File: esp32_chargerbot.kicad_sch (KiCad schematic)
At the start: 6 parts, among them J1 USB_C_Receptacle_USB2.0_16P, U1 AMS1117-3.3

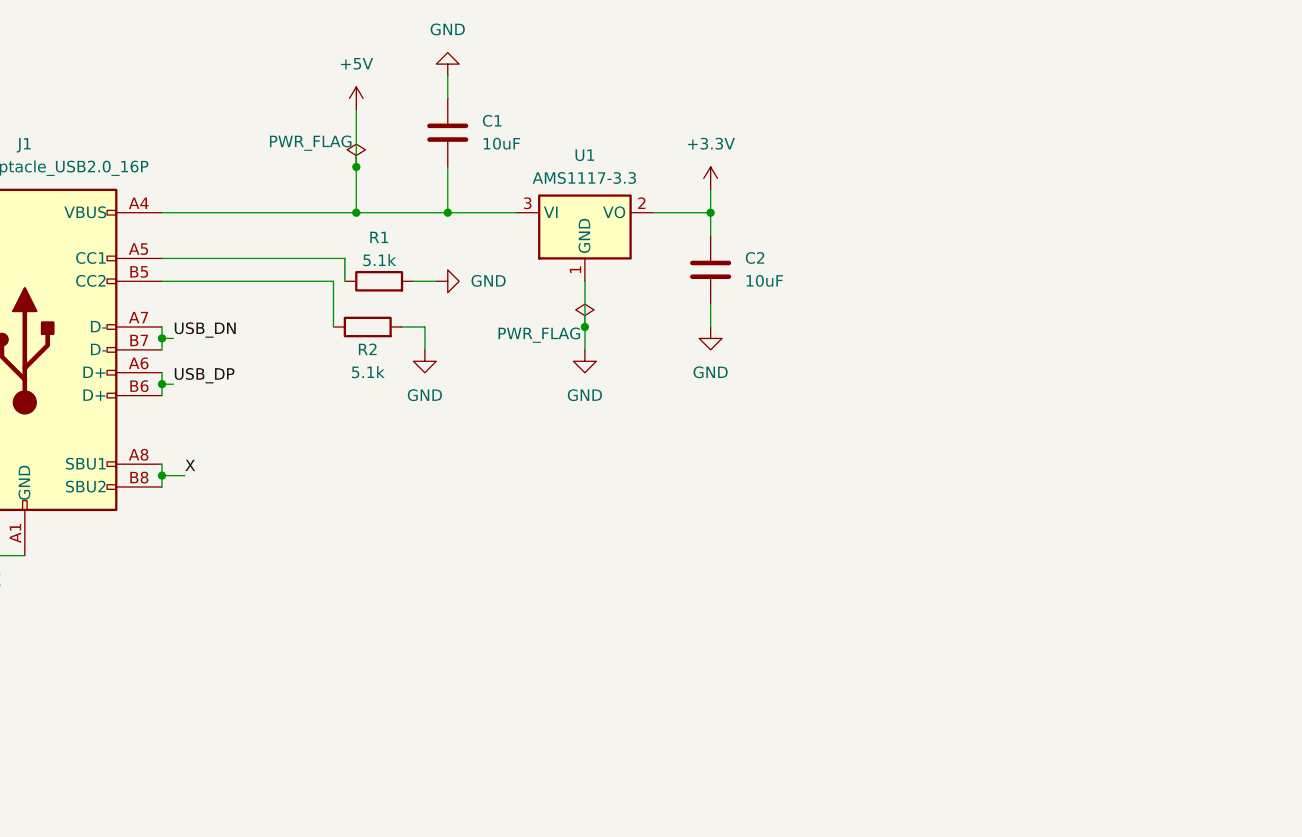
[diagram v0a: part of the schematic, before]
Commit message: ESP32-S3 power wiring, USB D+/D- fix
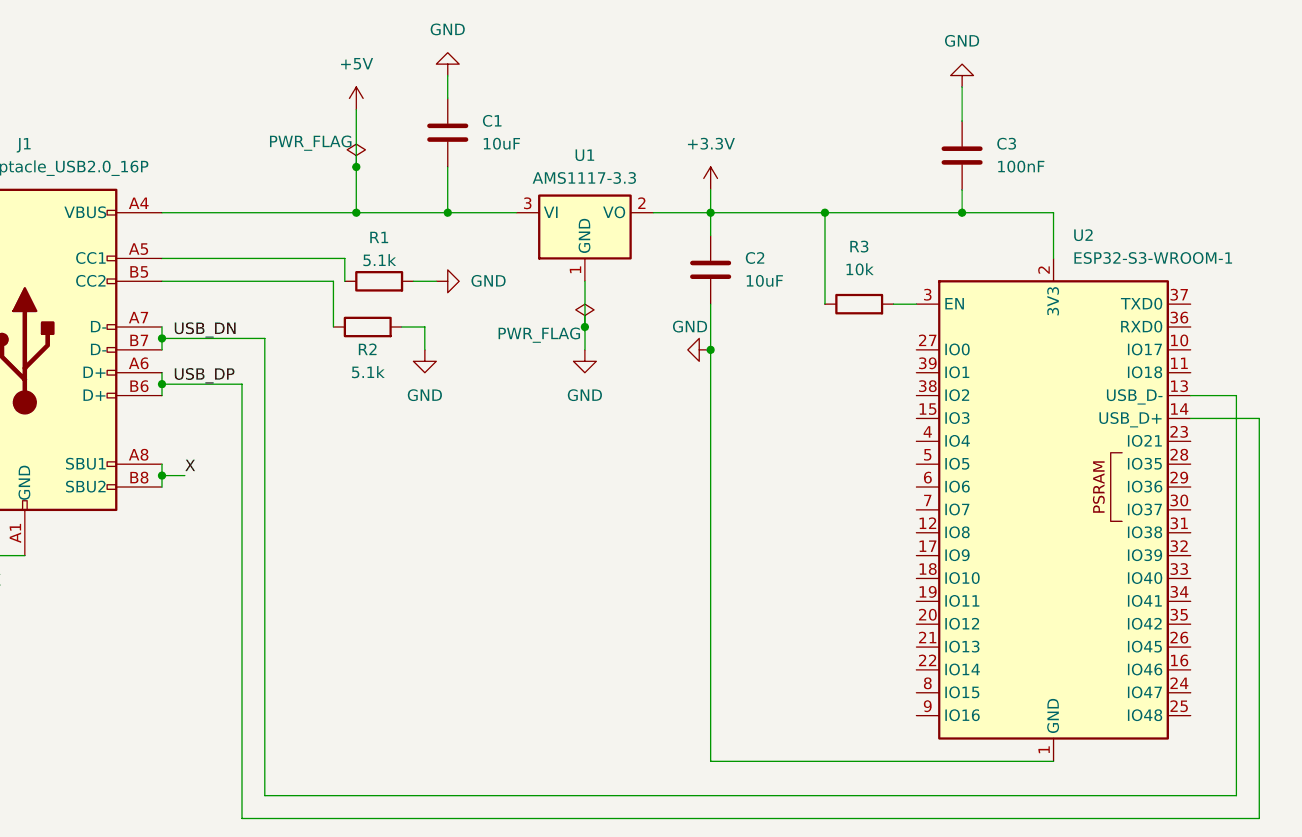
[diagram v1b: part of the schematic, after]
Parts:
- added C3: 100nF, symbol Device:C
- added R3: 10k, symbol Device:R
- added U2: ESP32-S3-WROOM-1, RF_Module:ESP32-S3-WROOM-1, symbol RF_Module:ESP32-S3-WROOM-1
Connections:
- net +3.3V: now also C3.1, R3.1, U2.2 (3V3)
- net GND: now also C3.2, U2.1 (GND), U2.40 (GND), U2.41 (GND)
- net USB_DN: now also U2.13 (USB_D-)
- net USB_DP: now also U2.14 (USB_D+)
- new net: R3.2, U2.3 (EN)

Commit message: MPU-6050 wiring complete, previous errors fixed
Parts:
- added C4: 0.1uF, symbol Device:C
- added C5: 2.2nF, symbol Device:C
- added C6: 10nF, symbol Device:C
- added R4: 10k, symbol Device:R
- added R5, R6: 4.7k, symbol Device:R
- added SW1, SW2: SW_Push, symbol Switch:SW_Push
- added U4: MPU-6050, Sensor_Motion:InvenSense_QFN-24_4x4mm_P0.5mm, symbol Sensor_Motion:MPU-6050
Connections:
- net +3.3V: now also C6.1, R4.2, R5.2, R6.2, U4.13 (VDD), U4.8 (VLOGIC)
- net GND: now also C4.1, C5.1, C6.2, SW1.1, SW2.1, U4.11 (FSYNC), U4.18 (GND), U4.9 (AD0)
- net at R3.2, U2.3 (EN): now also SW1.2
- net SDA: now reaches U2.12 (IO8)
- net SDA: now also R5.1, U4.24 (SDA)
- net SCL: now reaches U2.17 (IO9)
- net SCL: now also R6.1, U4.23 (SCL)
- net at U2.27 (IO0): now also R4.1, SW2.2
- net MPU_INT: now reaches U2.4 (IO4)
- net MPU_INT: now also U4.12 (INT)
- net X: no longer names the net of J1.A1 (GND), J1.A12 (GND), J1.B1 (GND), J1.B12 (GND)
- net X: no longer J1.A8 (SBU1), J1.B8 (SBU2), J1.SH (SHIELD)
- new net: C4.2, U4.10 (REGOUT)
- new net: C5.2, U4.20 (CPOUT)
- no-connect marks 0 -> 4
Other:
- moved on the sheet: C1, C2, C3, J1, R1, R2, R3, U1, U2

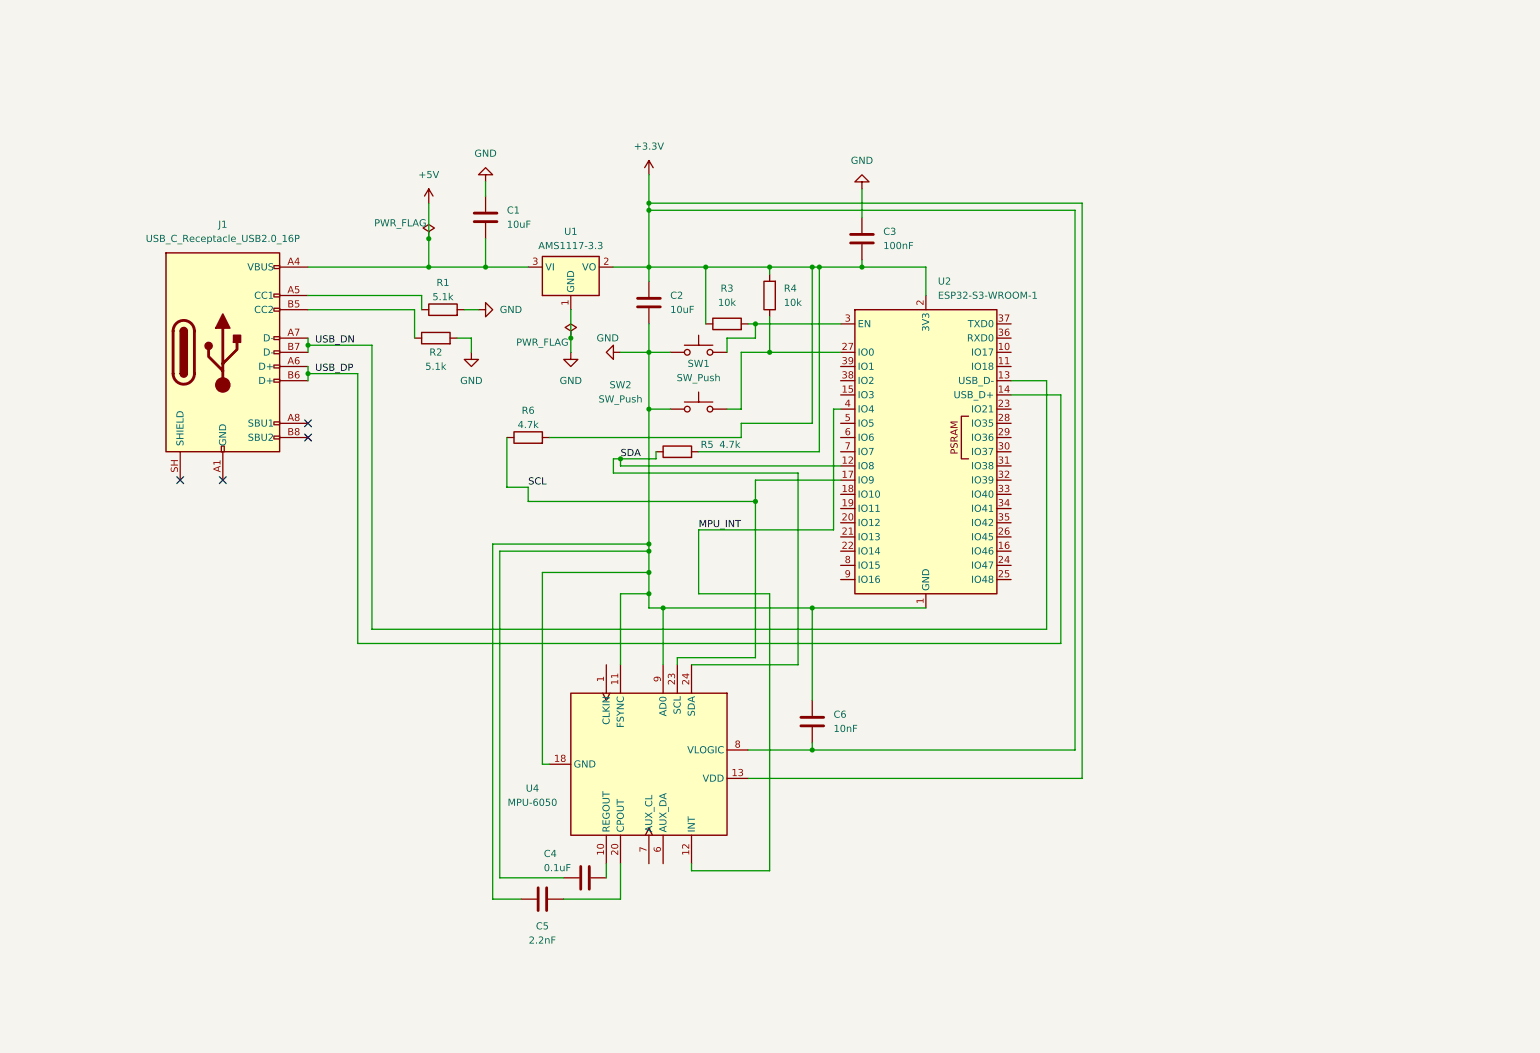
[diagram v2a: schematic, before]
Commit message: ToF sensors, PWM chip and Qi charging switch circuit added
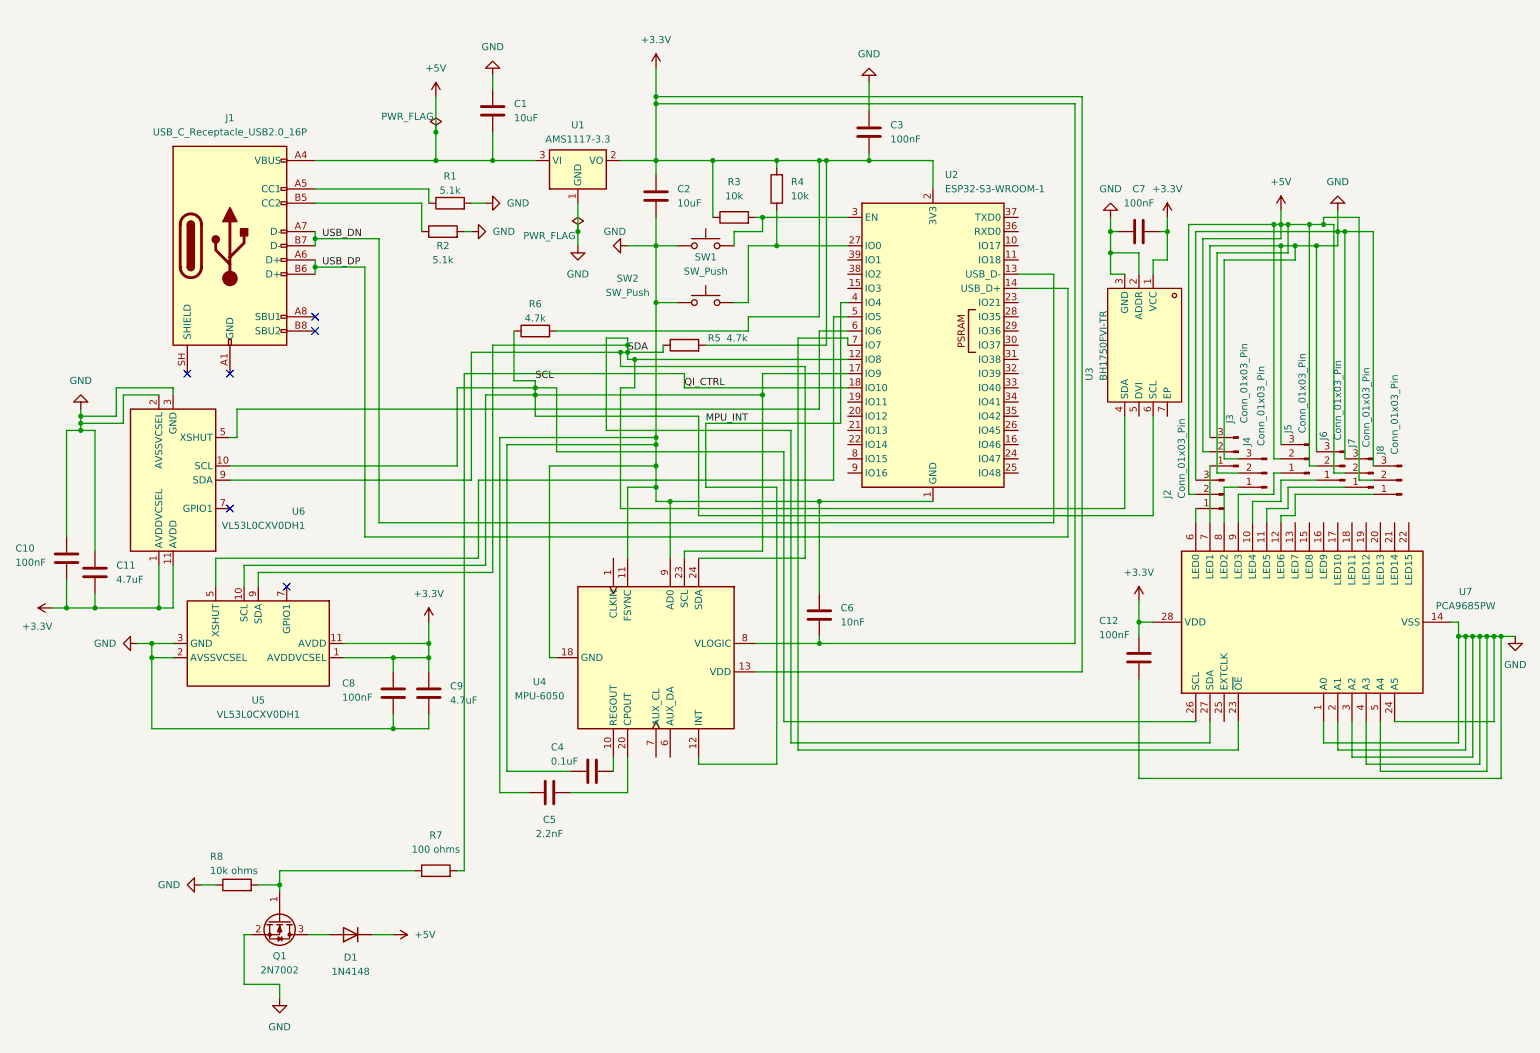
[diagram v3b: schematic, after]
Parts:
- added C10, C12, C7, C8: 100nF, symbol Device:C
- added C11, C9: 4.7uF, symbol Device:C
- added D1: 1N4148, Diode_THT:D_DO-35_SOD27_P7.62mm_Horizontal, symbol Diode:1N4148
- added J2, J3, J4, J5, J6, J7, J8: Conn_01x03_Pin, symbol Connector:Conn_01x03_Pin
- added Q1: 2N7002, Package_TO_SOT_SMD:SOT-23, symbol Transistor_FET:2N7002
- added R7: 100 ohms, symbol Device:R
- added R8: 10k ohms, symbol Device:R
- added U3: BH1750FVI-TR, easyeda2kicad:WSOF-6_L2.6-W1.6-P0.50-TL-EP, symbol easyeda2kicad:BH1750FVI-TR
- added U5, U6: VL53L0CXV0DH1, Sensor_Distance:ST_VL53L1x, symbol Sensor_Distance:VL53L0CXV0DH1
- added U7: PCA9685PW, Package_SO:TSSOP-28_4.4x9.7mm_P0.65mm, symbol Driver_LED:PCA9685PW
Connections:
- net +3.3V: now also C10.1, C11.2, C12.1, C7.1, C8.2, C9.1, U3.1 (VCC), U5.1 (AVDDVCSEL), U5.11 (AVDD), U6.1 (AVDDVCSEL), U6.11 (AVDD), U7.28 (VDD)
- net +5V: now also D1.1 (K), J2.2 (Pin_2), J3.2 (Pin_2), J4.2 (Pin_2), J5.2 (Pin_2), J6.2 (Pin_2), J7.2 (Pin_2), J8.2 (Pin_2)
- net GND: now also C10.2, C11.1, C12.2, C7.2, C8.1, C9.2, J2.3 (Pin_3), J3.3 (Pin_3), J4.3 (Pin_3), J5.3 (Pin_3), J6.3 (Pin_3), J7.3 (Pin_3), J8.3 (Pin_3), Q1.2 (S), R8.1, U3.2 (ADDR), U3.3 (GND), U5.12 (GND), U5.2 (AVSSVCSEL), U5.3 (GND), U5.4 (GND), U5.6 (GND), U6.12 (GND), U6.2 (AVSSVCSEL), U6.3 (GND), U6.4 (GND), U6.6 (GND), U7.1 (A0), U7.14 (VSS), U7.2 (A1), U7.24 (A5), U7.3 (A2), U7.4 (A3), U7.5 (A4)
- net SCL: now also U3.6 (SCL), U5.10 (SCL), U6.10 (SCL), U7.26 (SCL)
- net SDA: now also U3.4 (SDA), U5.9 (SDA), U6.9 (SDA), U7.27 (SDA)
- net QI_CTRL: now reaches U2.18 (IO10)
- net QI_CTRL: now also R7.2
- net at U2.5 (IO5): now also U5.5 (XSHUT)
- net at U2.6 (IO6): now also U6.5 (XSHUT)
- net at U2.7 (IO7): now also U7.23 (~{OE})
- new net: J6.1 (Pin_1), U7.10 (LED4)
- new net: J7.1 (Pin_1), U7.11 (LED5)
- new net: J8.1 (Pin_1), U7.12 (LED6)
- new net: J2.1 (Pin_1), U7.6 (LED0)
- new net: J3.1 (Pin_1), U7.7 (LED1)
- new net: J4.1 (Pin_1), U7.8 (LED2)
- new net: J5.1 (Pin_1), U7.9 (LED3)
- new net: Q1.1 (G), R7.1, R8.2
- new net: D1.2 (A), Q1.3 (D)
- no-connect marks 4 -> 6
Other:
- moved on the sheet: C1, C2, C3, C4, C5, C6, J1, R1, R2, R3, R4, R5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

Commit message: New symbols added to the schematic
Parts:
- added J10, J11, J12, J9: Conn_01x03_Pin, symbol Connector:Conn_01x03_Pin
- added LED1, LED2: TJ-S1615SW6TGLCCSRGB-A5, easyeda2kicad:LED-ARRAY-SMD_4P-L1.6-W1.5-BL-FD-1, symbol easyeda2kicad:TJ-S1615SW6TGLCCSRGB-A5
- added R10, R11, R12, R13, R14, R9: 330 ohms, symbol Device:R
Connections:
- net +5V: now also J10.2 (Pin_2), J11.2 (Pin_2), J12.2 (Pin_2), J9.2 (Pin_2)
- net GND: now also J10.3 (Pin_3), J11.3 (Pin_3), J12.3 (Pin_3), J9.3 (Pin_3), LED1.4, LED2.4
- net at U7.13 (LED7): now also J9.1 (Pin_1)
- net at U7.15 (LED8): now also J10.1 (Pin_1)
- net at U7.16 (LED9): now also J11.1 (Pin_1)
- net at U7.17 (LED10): now also J12.1 (Pin_1)
- net at U2.22 (IO14): now also R11.1, R14.1
- net at U2.35 (IO42): now also R12.1, R9.1
- net at U2.8 (IO15): now also R10.1, R13.1
- new net: LED1.1 (G), R12.2
- new net: LED1.2 (B), R13.2
- new net: LED1.3 (R), R14.2
- new net: LED2.1 (G), R9.2
- new net: LED2.2 (B), R10.2
- new net: LED2.3 (R), R11.2
- no-connect marks 6 -> 40
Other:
- moved on the sheet: C1, C10, C11, C12, C2, C3, C4, C5, C6, C7, C8, C9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

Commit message: Remaining symbols & footprints for all symbols added to the schematic
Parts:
- added C13: C_Polarized_1000uF, Capacitor_SMD:CP_Elec_10x10, symbol Device:C_Polarized
- added C14, C15, C16: 100nF, Capacitor_SMD:C_0402_1005Metric, symbol Device:C
- added J13: Conn_01x02_Pin, Connector_PinHeader_2.54mm:PinHeader_1x02_P2.54mm_Vertical, symbol Connector:Conn_01x02_Pin
- added MK1, MK2: ICS-43434, Sensor_Audio:InvenSense_ICS-43434-6_3.5x2.65mm, symbol Sensor_Audio:ICS-43434
- C1, C2: footprint (none) -> Capacitor_SMD:C_0805_2012Metric
- C10, C11, C12, C3, C4, C5, C6, C7, C8, C9: footprint (none) -> Capacitor_SMD:C_0402_1005Metric
- J1: value USB_C_Receptacle_USB2.0_16P -> TYPE-C-31-M-12A; footprint (none) -> easyeda2kicad:USB-C-SMD_TYPE-C-31-M-12A; symbol Connector:USB_C_Receptacle_USB2.0_16P -> easyeda2kicad:TYPE-C-31-M-12A; LCSC Part (none) -> C5337088; MPN (none) -> TYPE-C-31-M-12A; Manufacturer (none) -> 韩国韩荣
- J10, J11, J12, J2, J3, J4, J5, J6, J7, J8, J9: footprint (none) -> Connector_PinHeader_2.54mm:PinHeader_1x03_P2.54mm_Vertical
- R1, R10, R11, R12, R13, R14, R2, R3, R4, R5, R6, R7, R8, R9: footprint (none) -> Resistor_SMD:R_0402_1005Metric
- SW1, SW2: footprint (none) -> Button_Switch_SMD:SW_SPST_TL3342
- U5, U6: footprint Sensor_Distance:ST_VL53L1x -> OptoDevice:ST_VL53L0X
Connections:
- net +3.3V: now also C14.1, C15.1, C16.2, MK1.5 (VDD), MK2.2 (LR), MK2.5 (VDD)
- net +5V: now also J1.A4/B9 (VBUS), J1.B4/A9 (VBUS), C13.1, J13.2 (Pin_2); no longer J1.A4 (VBUS), J1.A9 (VBUS), J1.B4 (VBUS), J1.B9 (VBUS)
- net GND: now also J1.1 (EH), J1.A1/B12 (GND), J1.B1/A12 (GND), C13.2, C14.2, C15.2, C16.1, MK1.2 (LR), MK1.3 (GND), MK2.3 (GND)
- net at D1.2 (A), Q1.3 (D): now also J13.1 (Pin_1)
- net MIC_WS: now reaches U2.19 (IO11)
- net MIC_WS: now also MK1.1 (WS), MK2.1 (WS)
- net MIC_SCK: now reaches U2.20 (IO12)
- net MIC_SCK: now also MK1.4 (SCK), MK2.4 (SCK)
- net MIC_SD: now reaches U2.21 (IO13)
- net MIC_SD: now also MK1.6 (SD), MK2.6 (SD)
- no-connect marks 40 -> 35
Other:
- moved on the sheet: C5, C6, D1, Q1, R1, R2, R7, R8, SW2
